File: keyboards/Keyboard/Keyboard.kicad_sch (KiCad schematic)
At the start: 92 parts

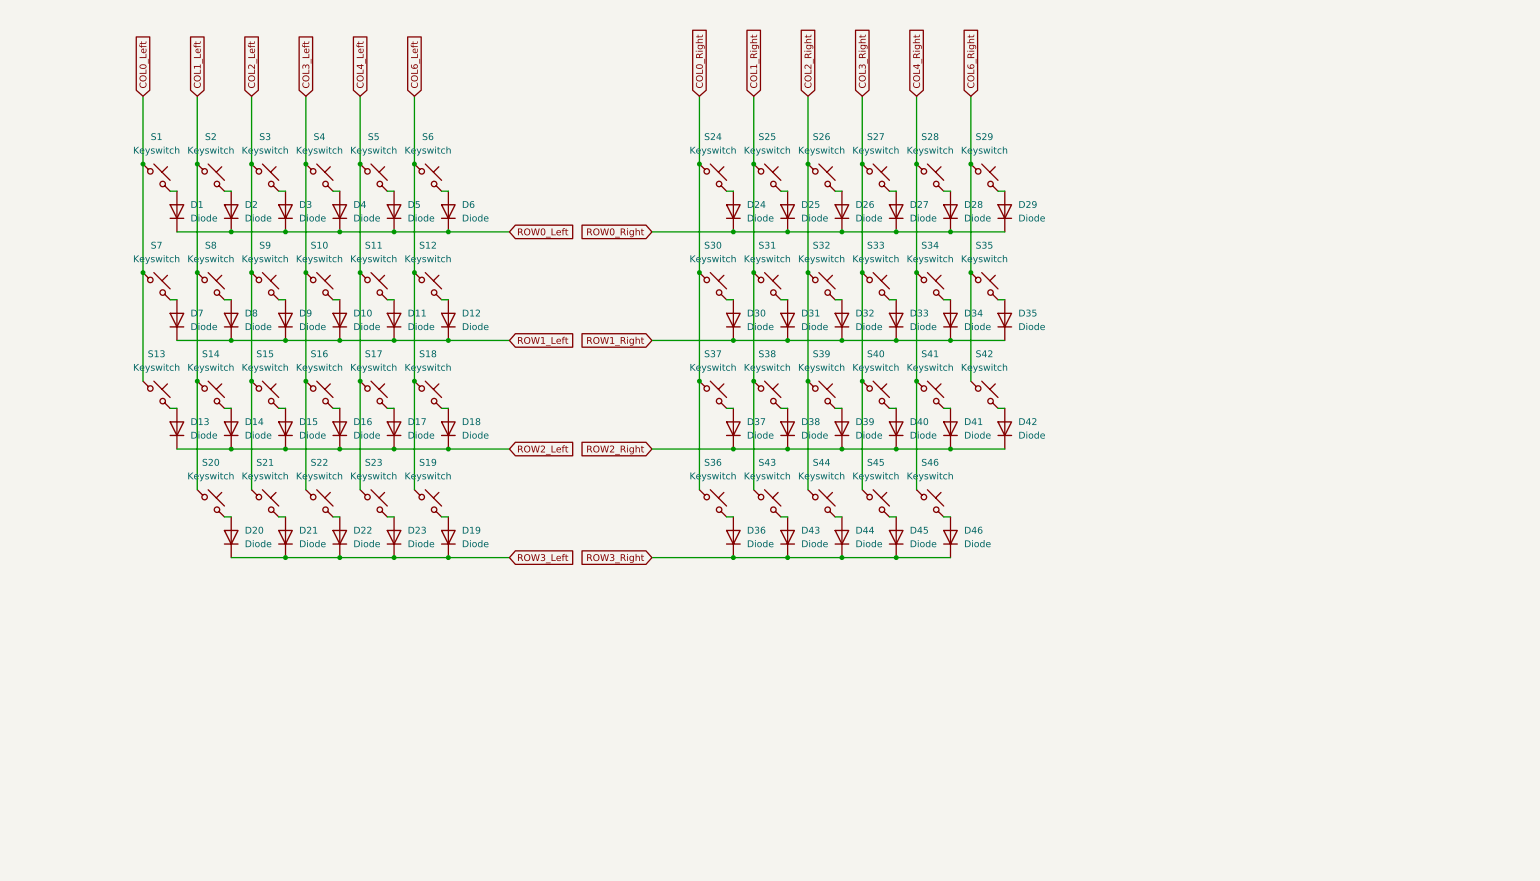
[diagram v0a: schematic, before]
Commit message: add TRRS Connection
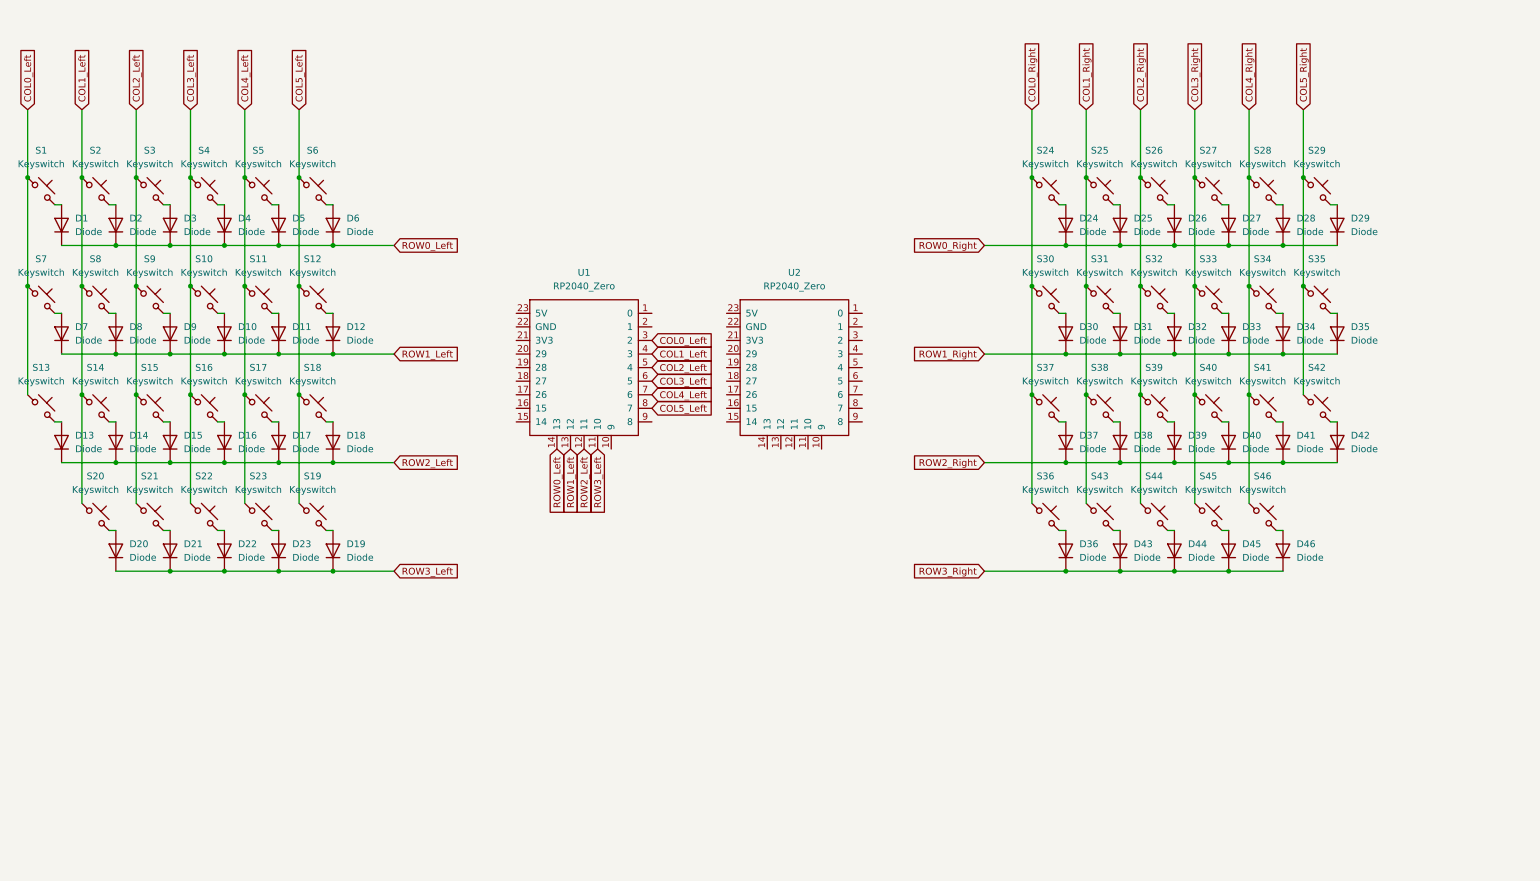
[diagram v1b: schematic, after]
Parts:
- added U1, U2: RP2040_Zero, ScottoKeebs_MCU:RP2040_Zero, symbol ScottoKeebs:MCU_RP2040_Zero
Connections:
- net COL0_Left: now also U1.3 (2)
- net COL1_Left: now also U1.4 (3)
- net COL2_Left: now also U1.5 (4)
- net COL3_Left: now also U1.6 (5)
- net COL4_Left: now also U1.7 (6)
- net ROW0_Left: now also U1.14 (13)
- net ROW1_Left: now also U1.13 (12)
- net ROW2_Left: now also U1.12 (11)
- net ROW3_Left: now also U1.11 (10)
- net COL6_Left renamed COL5_Left
- net COL5_Left: now also U1.8 (7)
- net COL6_Right renamed COL5_Right
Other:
- moved on the sheet: D1, D10, D11, D12, D13, D14, D15, D16, D17, D18, D19, D2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

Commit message: complete schematic design and edit pcb file
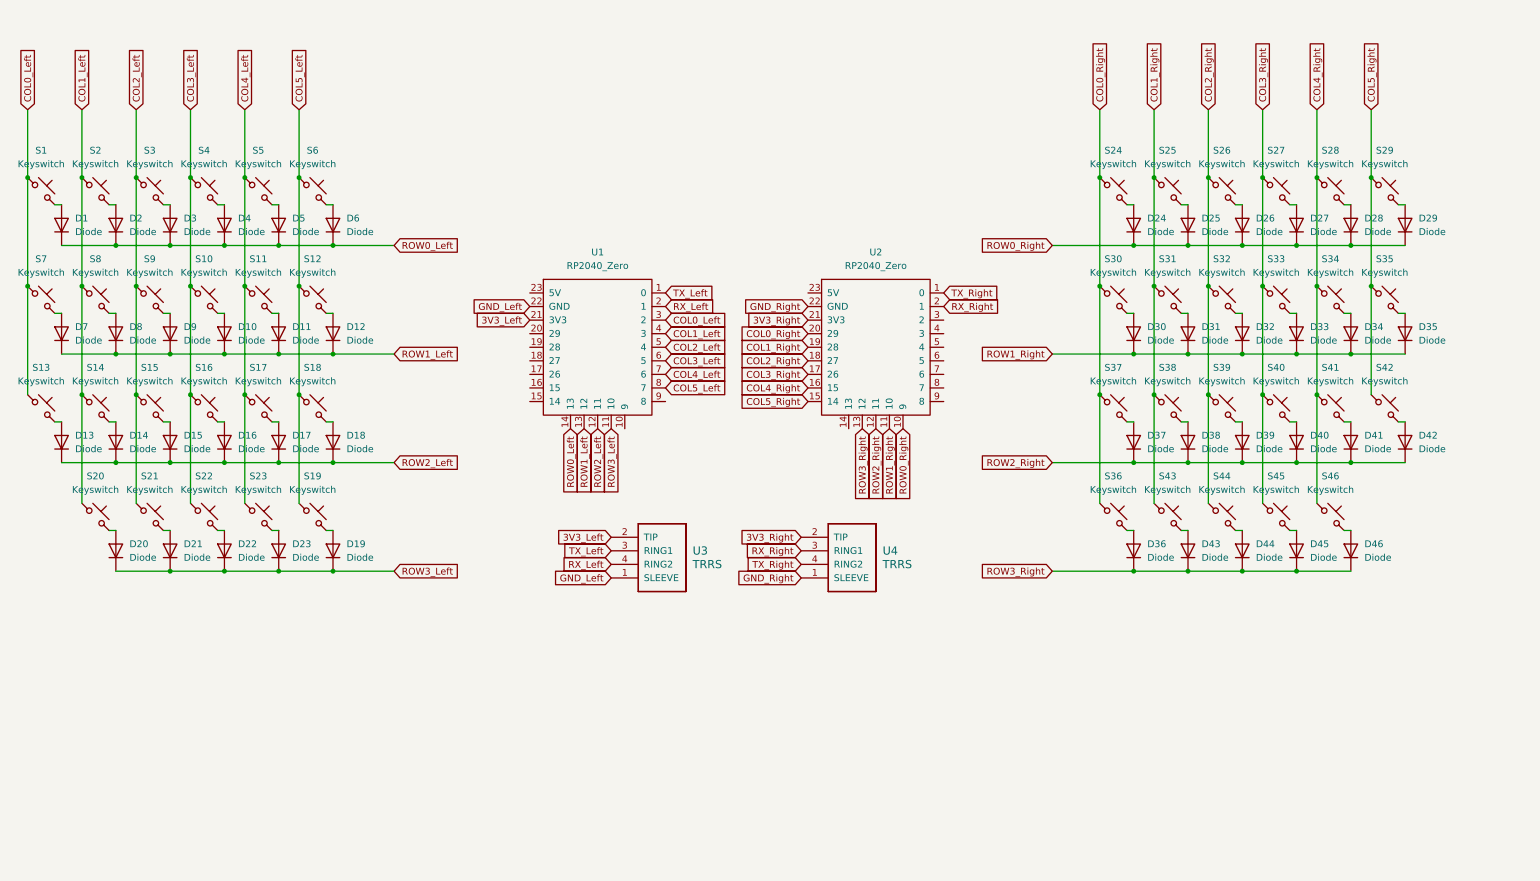
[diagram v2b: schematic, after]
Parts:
- added U3, U4: TRRS, ScottoKeebs_Components:TRRS_PJ-320A, symbol ScottoKeebs:Placeholder_TRRS
- D1, D10, D11, D12, D13, D14, D15, D16, D17, D18, D19, D2, D20, D21, D22, D23, D24, D25, D26, D27, D28, D29, D3, D30, D31, D32, D33, D34, D35, D36, D37, D38, D39, D4, D40, D41, D42, D43, D44, D45, D46, D5, D6, D7, D8, D9: footprint (none) -> ScottoKeebs_Components:Diode_DO-35
- S1, S10, S11, S12, S13, S14, S15, S16, S17, S18, S19, S2, S20, S21, S22, S23, S24, S25, S26, S27, S28, S29, S3, S30, S31, S32, S33, S34, S35, S36, S37, S38, S39, S4, S40, S41, S42, S43, S44, S45, S46, S5, S6, S7, S8, S9: footprint (none) -> ScottoKeebs_MX:MX_PCB_1.00u
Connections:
- net COL0_Right: now also U2.20 (29)
- net COL1_Right: now also U2.19 (28)
- net COL2_Right: now also U2.18 (27)
- net COL3_Right: now also U2.17 (26)
- net COL4_Right: now also U2.16 (15)
- net COL5_Right: now also U2.15 (14)
- net ROW0_Right: now also U2.10 (9)
- net ROW1_Right: now also U2.11 (10)
- net ROW2_Right: now also U2.12 (11)
- net ROW3_Right: now also U2.13 (12)
- net TX_Right: now reaches U2.1 (0)
- net TX_Right: now also U4.4 (RING2)
- net RX_Right: now reaches U2.2 (1)
- net RX_Right: now also U4.3 (RING1)
- net 3V3_Right: now reaches U2.21 (3V3)
- net 3V3_Right: now also U4.2 (TIP)
- net GND_Right: now reaches U2.22 (GND)
- net GND_Right: now also U4.1 (SLEEVE)
- net TX_Left: now reaches U1.1 (0)
- net TX_Left: now also U3.3 (RING1)
- net RX_Left: now reaches U1.2 (1)
- net RX_Left: now also U3.4 (RING2)
- net 3V3_Left: now reaches U1.21 (3V3)
- net 3V3_Left: now also U3.2 (TIP)
- net GND_Left: now reaches U1.22 (GND)
- net GND_Left: now also U3.1 (SLEEVE)
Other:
- moved on the sheet: D24, D25, D26, D27, D28, D29, D30, D31, D32, D33, D34, D35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

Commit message: add PCB routing, Mounting Hole
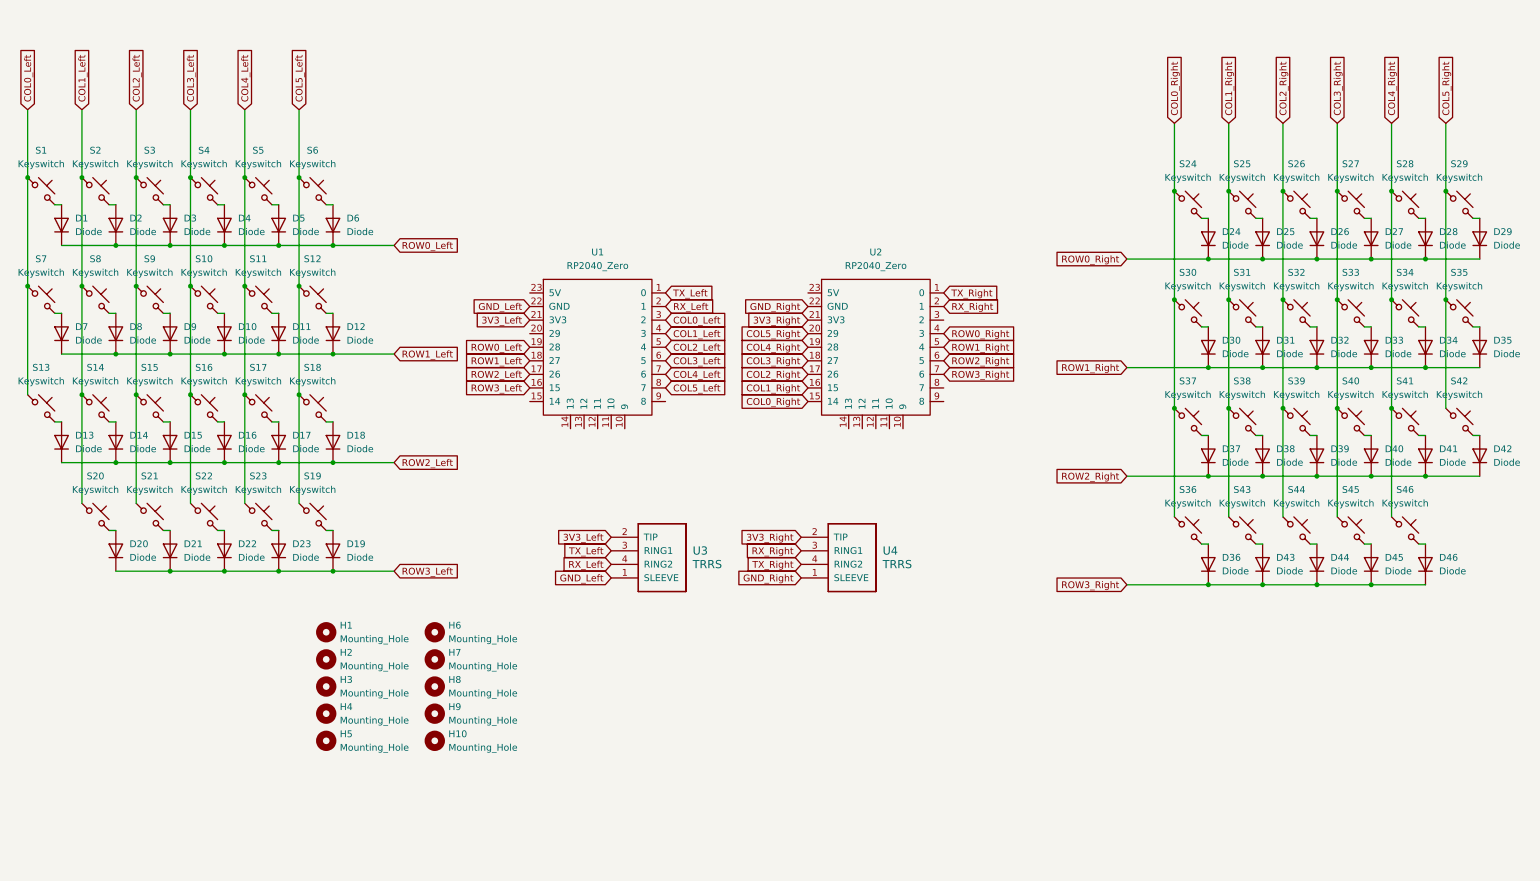
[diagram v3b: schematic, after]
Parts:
- added H1, H10, H2, H3, H4, H5, H6, H7, H8, H9: Mounting_Hole, MountingHole:MountingHole_2.2mm_M2, symbol ScottoKeebs:Placeholder_Mounting_Hole
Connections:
- net COL0_Right: now also U2.15 (14); no longer U2.20 (29)
- net COL1_Right: now also U2.16 (15); no longer U2.19 (28)
- net COL2_Right: now also U2.17 (26); no longer U2.18 (27)
- net COL3_Right: now also U2.18 (27); no longer U2.17 (26)
- net COL4_Right: now also U2.19 (28); no longer U2.16 (15)
- net COL5_Right: now also U2.20 (29); no longer U2.15 (14)
- net ROW0_Left: now also U1.19 (28); no longer U1.14 (13)
- net ROW0_Right: now also U2.4 (3); no longer U2.10 (9)
- net ROW1_Left: now also U1.18 (27); no longer U1.13 (12)
- net ROW1_Right: now also U2.5 (4); no longer U2.11 (10)
- net ROW2_Left: now also U1.17 (26); no longer U1.12 (11)
- net ROW2_Right: now also U2.6 (5); no longer U2.12 (11)
- net ROW3_Left: now also U1.16 (15); no longer U1.11 (10)
- net ROW3_Right: now also U2.7 (6); no longer U2.13 (12)
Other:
- moved on the sheet: D24, D25, D26, D27, D28, D29, D30, D31, D32, D33, D34, D35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

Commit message: keyboard pcb design complete
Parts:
- added H11, H12: Mounting_Hole, MountingHole:MountingHole_2.2mm_M2, symbol ScottoKeebs:Placeholder_Mounting_Hole
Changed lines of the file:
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@@
+    )
+  )
+  (symbol (lib_id "ScottoKeebs:Placeholder_Mounting_Hole") (at 100.33 162.56 0) (unit 1)
+    (in_bom yes) (on_board yes) (dnp no) (fields_autoplaced)
+    (property "Reference" "H12" (at 102.87 161.29 0)
+      (effects (font (size 1.27 1.27)) (justify left))
+    )
+    (property "Value" "Mounting_Hole" (at 102.87 163.83 0)
+      (effects (font (size 1.27 1.27)) (justify left))
+    )
+    (property "Footprint" "MountingHole:MountingHole_2.2mm_M2" (at 100.33 162.56 0)
+      (effects (font (size 1.27 1.27)) hide)
+    )
+    (property "Datasheet" "~" (at 100.33 162.56 0)
+      (effects (font (size 1.27 1.27)) hide)
+    )
+    (instances
+      (project "Keyboard"
+        (path "/63a9847b-cdc2-4bdd-9a63-560a857f6935"
+          (reference "H12") (unit 1)
+        )
+      )
     )
   )
@@
         )
       )
+    )
+  )
+  (symbol (lib_id "ScottoKeebs:Placeholder_Mounting_Hole") (at 78.74 161.29 0) (unit 1)
+    (in_bom yes) (on_board yes) (dnp no) (fields_autoplaced)
+    (property "Reference" "H11" (at 81.28 160.02 0)
+      (effects (font (size 1.27 1.27)) (justify left))
+    )
+    (property "Value" "Mounting_Hole" (at 81.28 162.56 0)
+      (effects (font (size 1.27 1.27)) (justify left))
+    )
+    (property "Footprint" "MountingHole:MountingHole_2.2mm_M2" (at 78.74 161.29 0)
+      (effects (font (size 1.27 1.27)) hide)
+    )
+    (property "Datasheet" "~" (at 78.74 161.29 0)
+      (effects (font (size 1.27 1.27)) hide)
+    )
+    (instances
+      (project "Keyboard"
+        (path "/63a9847b-cdc2-4bdd-9a63-560a857f6935"
+          (reference "H11") (unit 1)
+        )
+      )

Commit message: edit pcb file
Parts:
- added H13, H14, H15, H16: Mounting_Hole, MountingHole:MountingHole_2.2mm_M2, symbol ScottoKeebs:Placeholder_Mounting_Hole
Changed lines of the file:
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@@
+    )
+  )
+  (symbol (lib_id "ScottoKeebs:Placeholder_Mounting_Hole") (at 78.74 168.91 0) (unit 1)
+    (in_bom yes) (on_board yes) (dnp no) (fields_autoplaced)
+    (property "Reference" "H13" (at 81.28 167.64 0)
+      (effects (font (size 1.27 1.27)) (justify left))
+    )
+    (property "Value" "Mounting_Hole" (at 81.28 170.18 0)
+      (effects (font (size 1.27 1.27)) (justify left))
+    )
+    (property "Footprint" "MountingHole:MountingHole_2.2mm_M2" (at 78.74 168.91 0)
+      (effects (font (size 1.27 1.27)) hide)
+    )
+    (property "Datasheet" "~" (at 78.74 168.91 0)
+      (effects (font (size 1.27 1.27)) hide)
+    )
+    (instances
+      (project "Keyboard"
+        (path "/63a9847b-cdc2-4bdd-9a63-560a857f6935"
+          (reference "H13") (unit 1)
+        )
+      )
     )
   )
@@
         (path "/63a9847b-cdc2-4bdd-9a63-560a857f6935"
           (reference "D3") (unit 1)
+        )
+      )
+    )
+  )
+  (symbol (lib_id "ScottoKeebs:Placeholder_Mounting_Hole") (at 100.33 176.53 0) (unit 1)
+    (in_bom yes) (on_board yes) (dnp no) (fields_autoplaced)
+    (property "Reference" "H16" (at 102.87 175.26 0)
+      (effects (font (size 1.27 1.27)) (justify left))
+    )
+    (property "Value" "Mounting_Hole" (at 102.87 177.8 0)
+      (effects (font (size 1.27 1.27)) (justify left))
+    )
+    (property "Footprint" "MountingHole:MountingHole_2.2mm_M2" (at 100.33 176.53 0)
+      (effects (font (size 1.27 1.27)) hide)
+    )
+    (property "Datasheet" "~" (at 100.33 176.53 0)
+      (effects (font (size 1.27 1.27)) hide)
+    )
+    (instances
+      (project "Keyboard"
+        (path "/63a9847b-cdc2-4bdd-9a63-560a857f6935"
+          (reference "H16") (unit 1)
+        )
+      )
+    )
+  )
+  (symbol (lib_id "ScottoKeebs:Placeholder_Mounting_Hole") (at 78.74 175.26 0) (unit 1)
+    (in_bom yes) (on_board yes) (dnp no) (fields_autoplaced)
+    (property "Reference" "H15" (at 81.28 173.99 0)
+      (effects (font (size 1.27 1.27)) (justify left))
+    )
+    (property "Value" "Mounting_Hole" (at 81.28 176.53 0)
+      (effects (font (size 1.27 1.27)) (justify left))
+    )
+    (property "Footprint" "MountingHole:MountingHole_2.2mm_M2" (at 78.74 175.26 0)
+      (effects (font (size 1.27 1.27)) hide)
+    )
+    (property "Datasheet" "~" (at 78.74 175.26 0)
+      (effects (font (size 1.27 1.27)) hide)
+    )
+    (instances
+      (project "Keyboard"
+        (path "/63a9847b-cdc2-4bdd-9a63-560a857f6935"
+          (reference "H15") (unit 1)
         )
       )
@@
         )
       )
+    )
+  )
+  (symbol (lib_id "ScottoKeebs:Placeholder_Mounting_Hole") (at 100.33 170.18 0) (unit 1)
+    (in_bom yes) (on_board yes) (dnp no) (fields_autoplaced)
+    (property "Reference" "H14" (at 102.87 168.91 0)
+      (effects (font (size 1.27 1.27)) (justify left))
+    )
+    (property "Value" "Mounting_Hole" (at 102.87 171.45 0)
+      (effects (font (size 1.27 1.27)) (justify left))
+    )
+    (property "Footprint" "MountingHole:MountingHole_2.2mm_M2" (at 100.33 170.18 0)
+      (effects (font (size 1.27 1.27)) hide)
+    )
+    (property "Datasheet" "~" (at 100.33 170.18 0)
+      (effects (font (size 1.27 1.27)) hide)
+    )
+    (instances
+      (project "Keyboard"
+        (path "/63a9847b-cdc2-4bdd-9a63-560a857f6935"
+          (reference "H14") (unit 1)
+        )
+      )
